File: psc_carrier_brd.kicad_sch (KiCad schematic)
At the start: 12 parts, among them J1 Conn_01x08_Pin, J2 Conn_01x05_Pin - 3.3v, J3 Conn_01x05_Pin - 5v, J4 6469028-1, J5 39301022, U1 WeMos_D1_mini, U5 OPA2197xDGK

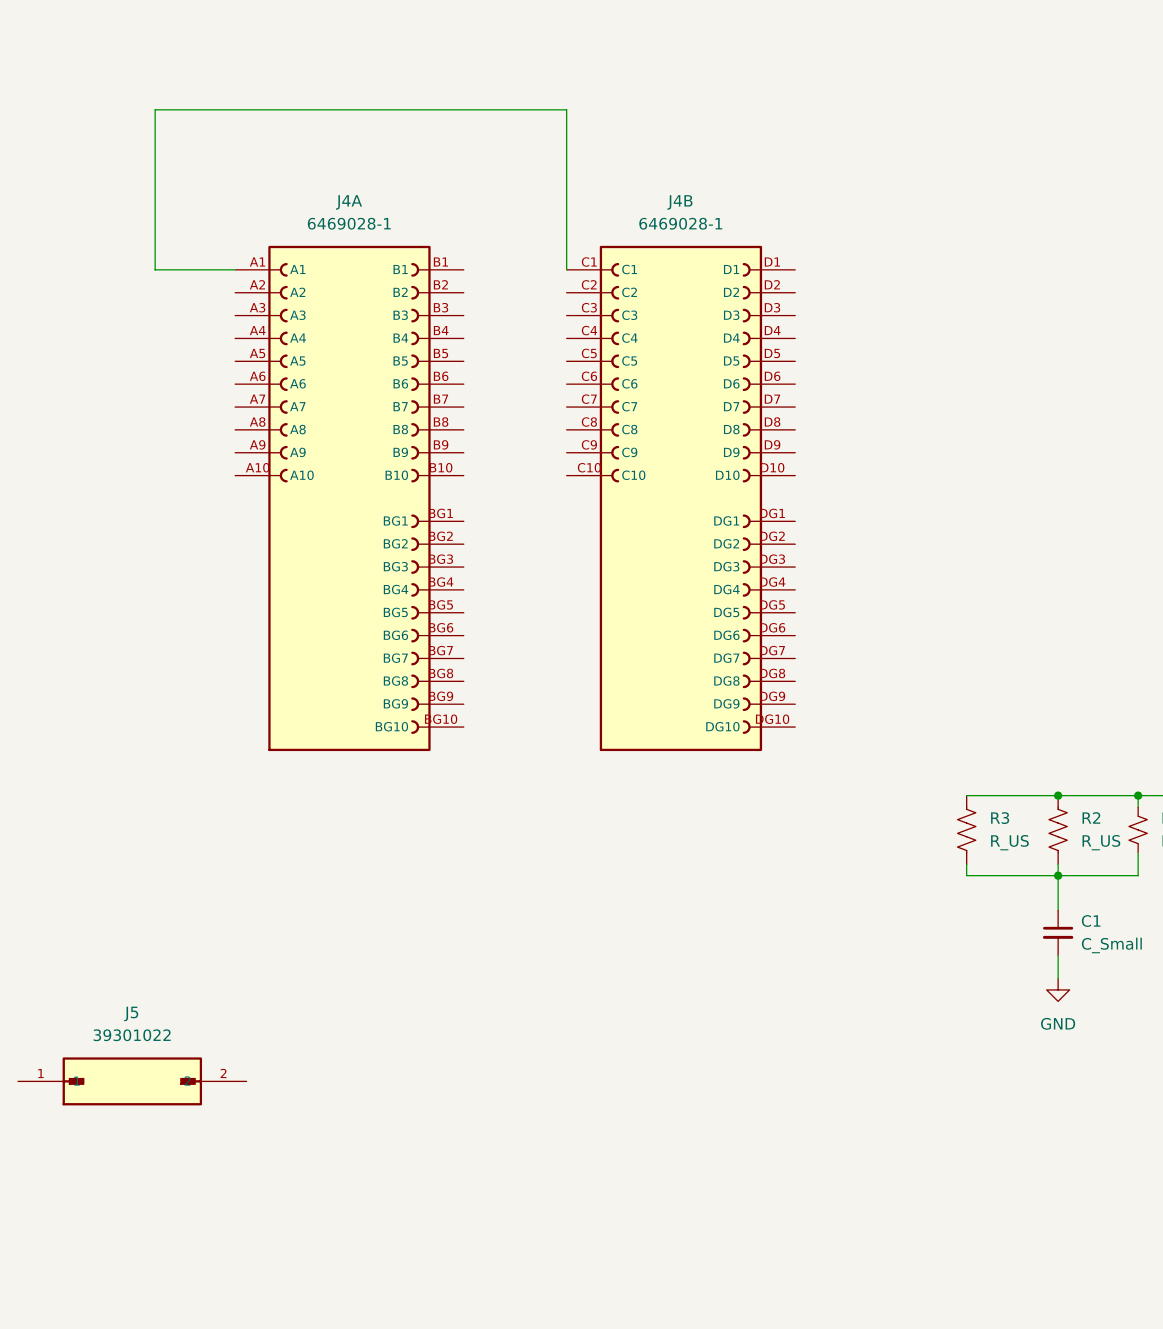
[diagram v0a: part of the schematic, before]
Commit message: Create 6469028-1 symbol
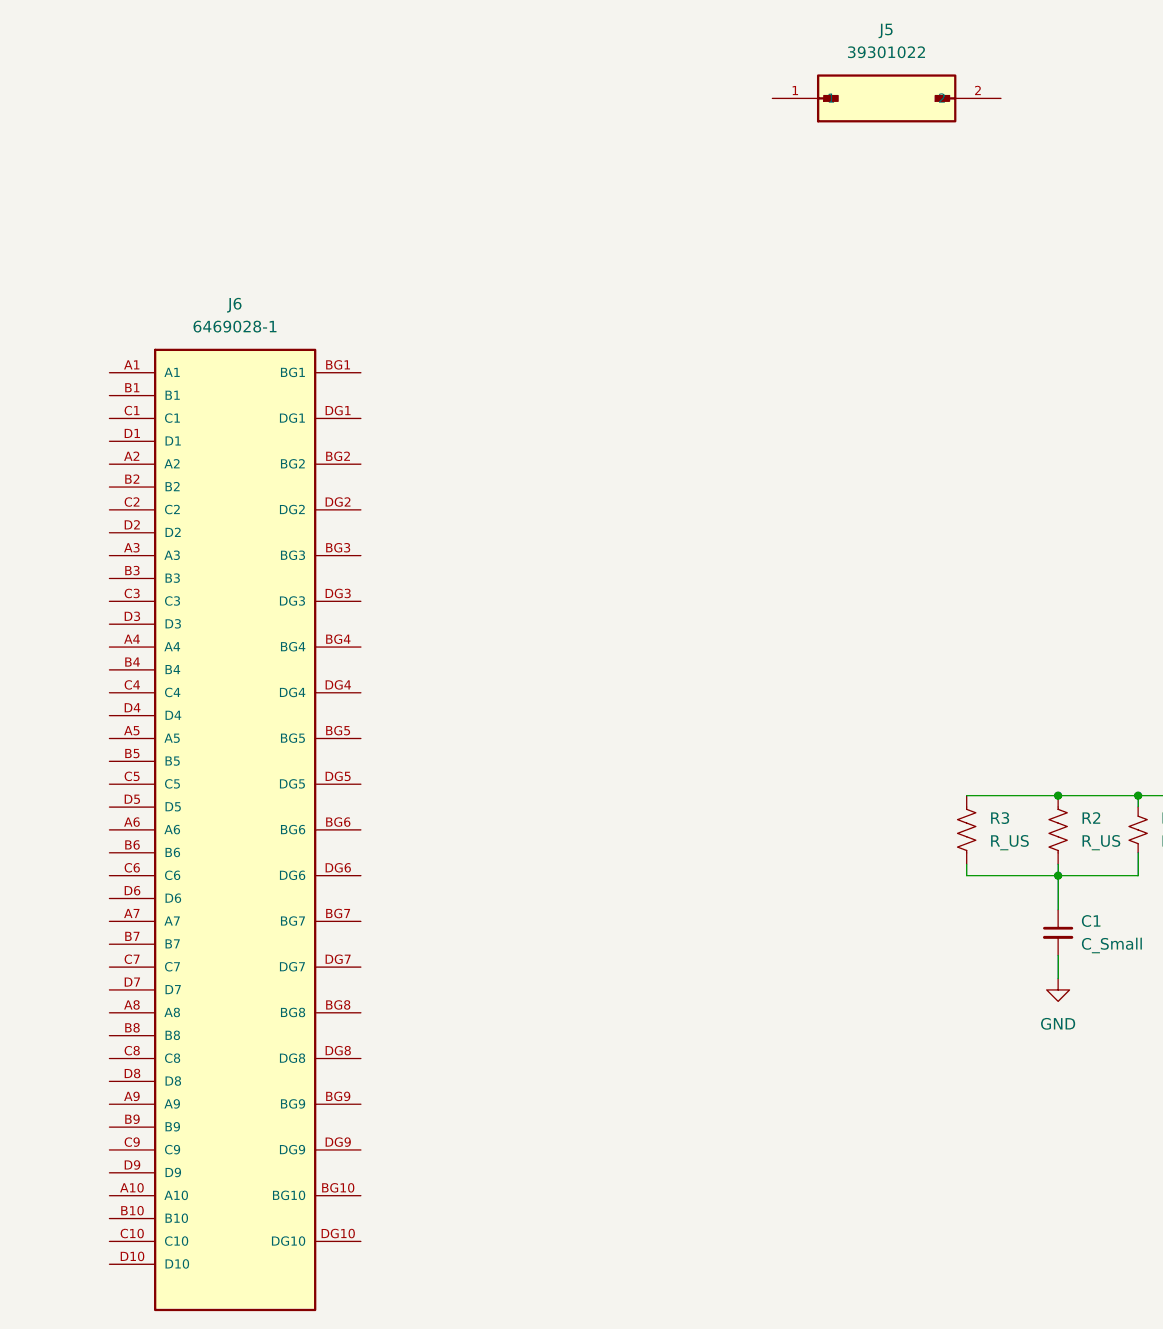
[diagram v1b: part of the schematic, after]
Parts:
- removed J4: 6469028-1, myparts:TE_6469028-1, symbol 6469028-1:6469028-1
- added J6: 6469028-1, 6469028-1:TE_6469028-1, symbol 6469028-1:6469028-1
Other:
- moved on the sheet: J5

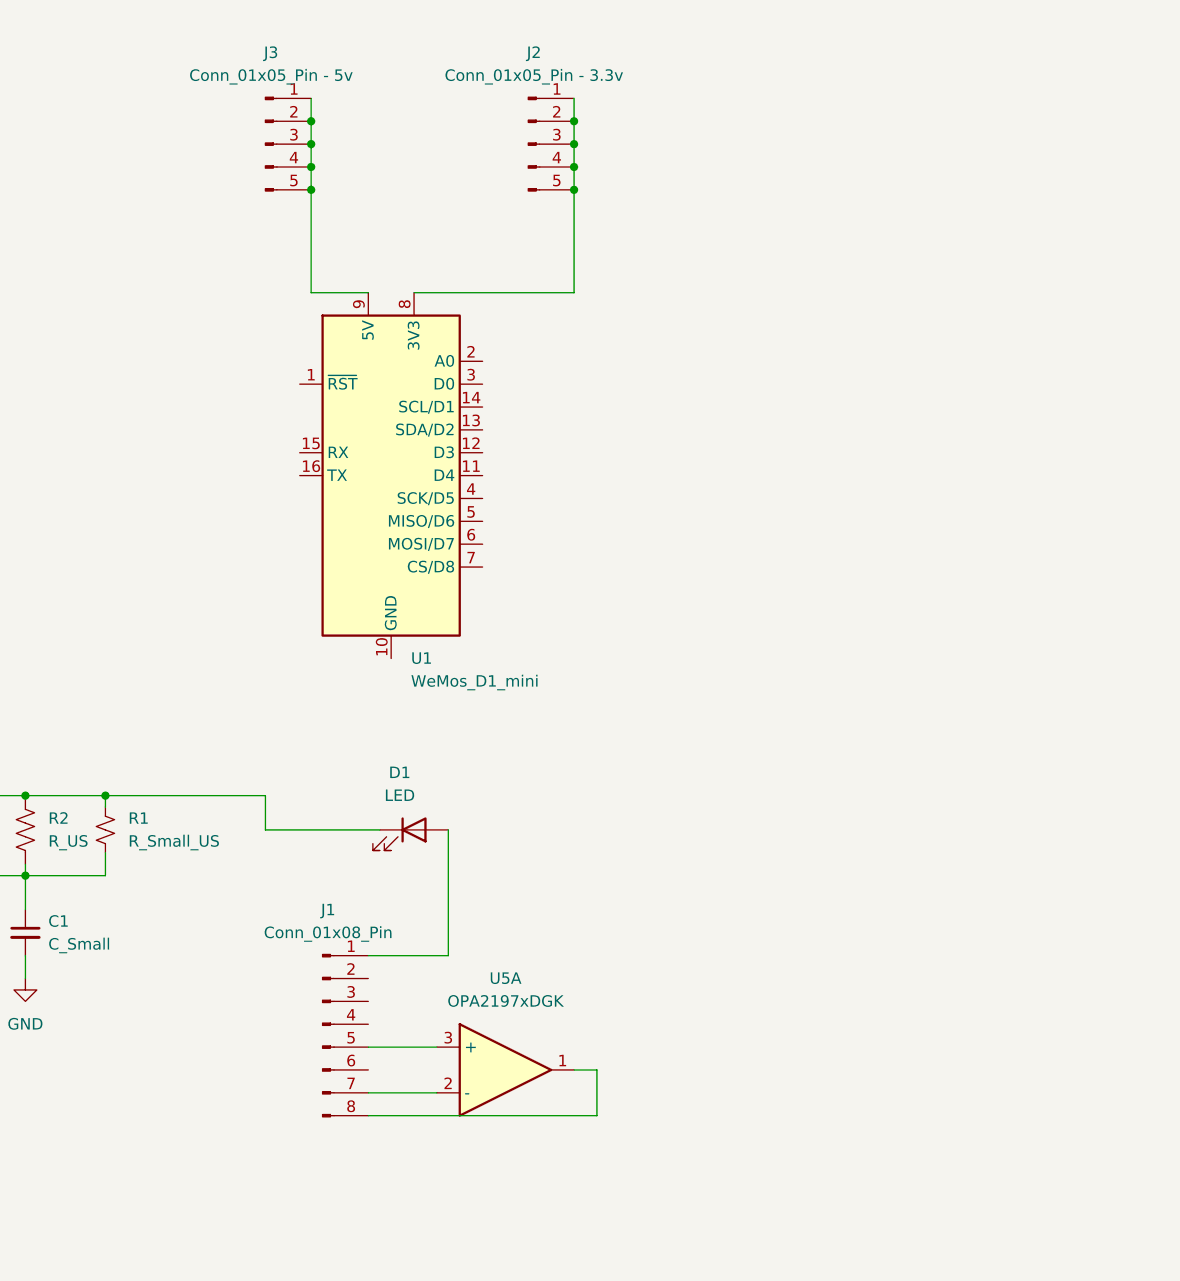
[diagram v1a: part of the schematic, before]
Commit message: Create custom NSLS2 worksheet
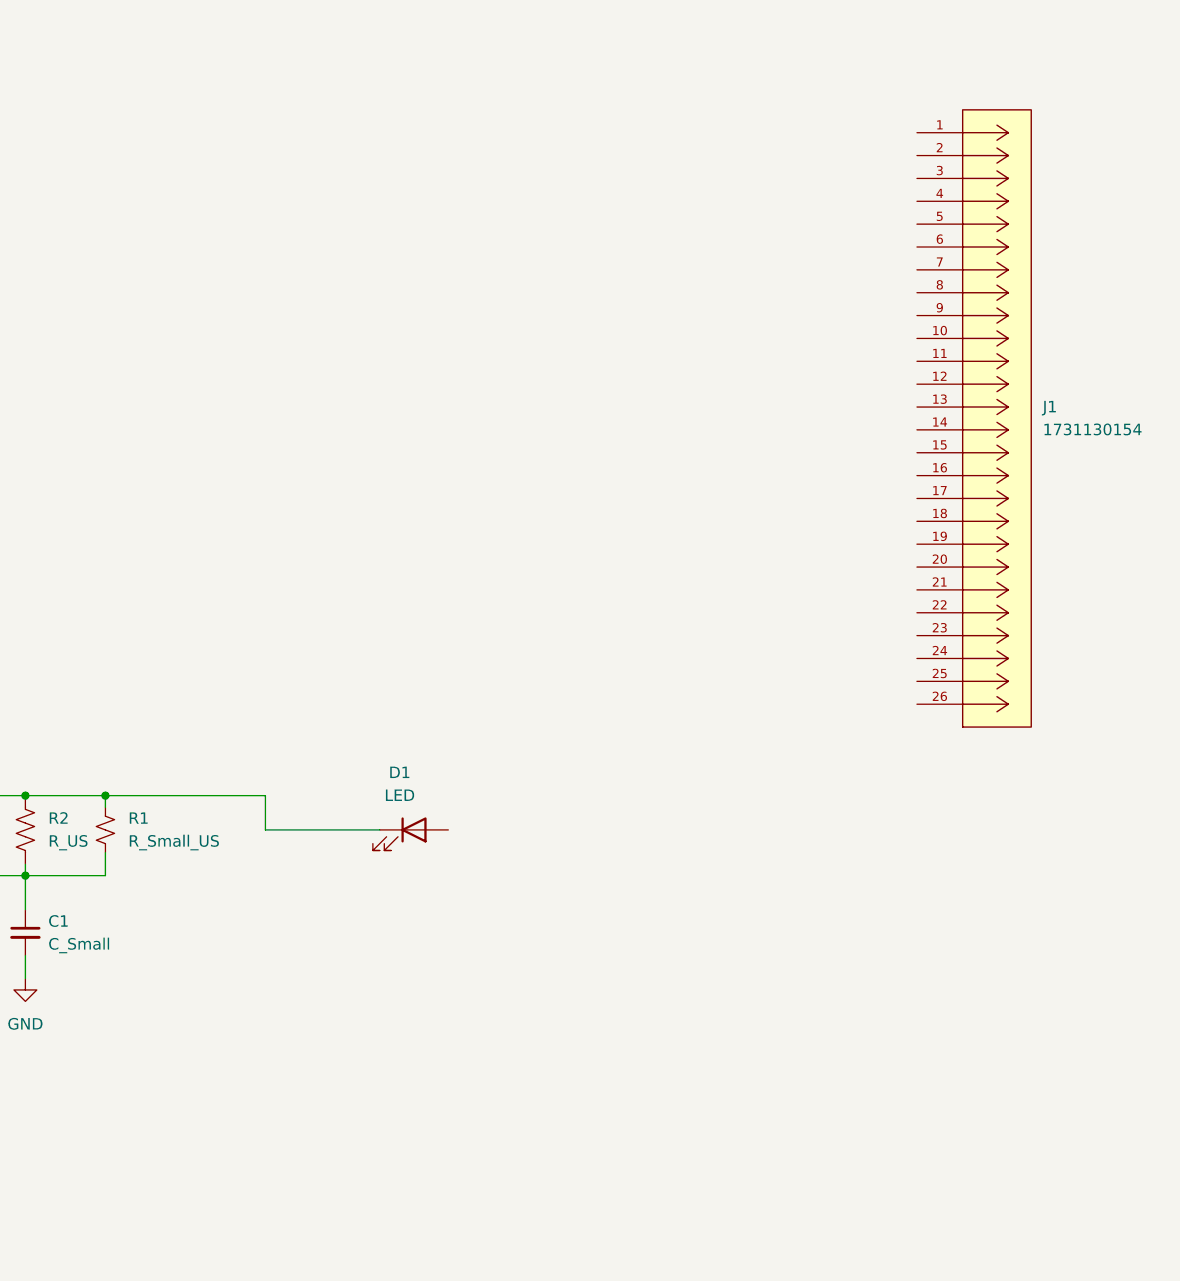
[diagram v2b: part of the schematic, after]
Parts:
- removed J1: Conn_01x08_Pin, Connector_PinHeader_2.54mm:PinHeader_1x08_P2.54mm_Vertical, symbol Connector:Conn_01x08_Pin
- removed J2: Conn_01x05_Pin - 3.3v, Connector_PinHeader_2.54mm:PinHeader_1x05_P2.54mm_Vertical_SMD_Pin1Left, symbol Connector:Conn_01x05_Pin
- removed J3: Conn_01x05_Pin - 5v, Connector_PinHeader_2.54mm:PinHeader_1x05_P2.54mm_Vertical_SMD_Pin1Left, symbol Connector:Conn_01x05_Pin
- removed U1: WeMos_D1_mini, Module:WEMOS_D1_mini_light, symbol MCU_Module:WeMos_D1_mini
- removed U5: OPA2197xDGK, Package_SO:VSSOP-8_3.0x3.0mm_P0.65mm, symbol Amplifier_Operational:OPA2197xDGK
- added J1: 1731130154, myparts:CONN_F15-26P135G0-5979_MOL, symbol 1731130154:1731130154
- J6: footprint 6469028-1:TE_6469028-1 -> myparts:TE_6469028-1

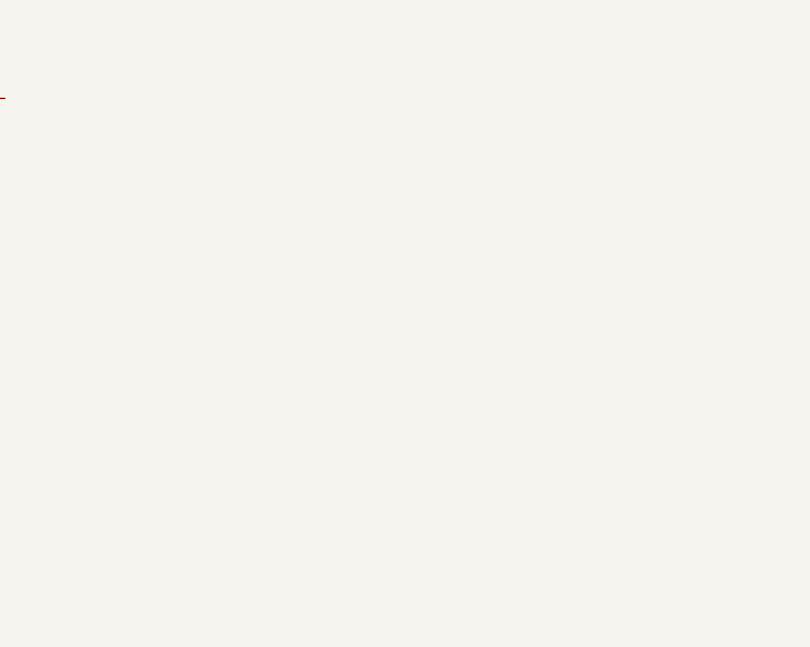
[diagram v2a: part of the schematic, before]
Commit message: Add symbol for PS connector
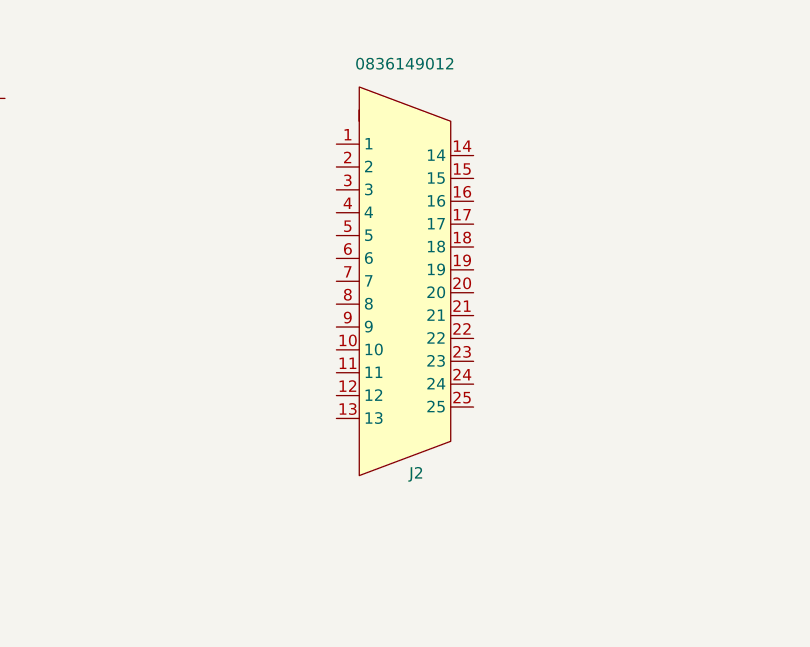
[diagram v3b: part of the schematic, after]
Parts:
- added J2: 0836149012, symbol 0836149012:0836149012
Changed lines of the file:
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@@
+	)
+	(symbol
+		(lib_id "0836149012:0836149012")
+		(at 207.01 40.64 0)
+		(unit 1)
+		(exclude_from_sim no)
+		(in_bom yes)
+		(on_board yes)
+		(dnp no)
+		(property "Reference" "J2"
+			(at 209.55 81.026 0)
+			(effects
+				(font
+					(size 1.27 1.27)
+				)
+			)
+		)
+		(property "Value" "0836149012"
+			(at 208.28 35.56 0)
+			(effects
+				(font
+					(size 1.27 1.27)
+				)
+			)
+		)
+		(property "Footprint" ""
+			(at 207.01 40.64 0)
+			(effects
+				(font
+					(size 1.27 1.27)
+				)
+				(hide yes)
+			)
+		)
+		(property "Datasheet" ""
+			(at 207.01 40.64 0)
+			(effects
+				(font
+					(size 1.27 1.27)
+				)
+				(hide yes)
+			)
+		)
+		(property "Description" ""
+			(at 207.01 40.64 0)
+			(effects
+				(font
+					(size 1.27 1.27)
+				)
+				(hide yes)
+			)
+		)
+		(pin "2"
+		)
+		(pin "25"
+		)
+		(pin "9"
+		)
+		(pin "4"
+		)
+		(pin "1"
+		)
+		(pin "10"
+		)
+		(pin "17"
+		)
+		(pin "22"
+		)
+		(pin "5"
+		)
+		(pin "3"
+		)
+		(pin "20"
+		)
+		(pin "6"
+		)
+		(pin "8"
+		)
+		(pin "24"
+		)
+		(pin "23"
+		)
+		(pin "21"
+		)
+		(pin "18"
+		)
+		(pin "19"
+		)
+		(pin "15"
+		)
+		(pin "12"
+		)
+		(pin "14"
+		)
+		(pin "13"
+		)
+		(pin "11"
+		)
+		(pin "16"
+		)
+		(pin "7"
+		)
+		(instances
+			(project ""
+				(path "/40891cc8-bf64-41f4-8f69-a607d7b280eb"
+					(reference "J2")
+					(unit 1)
+				)
+			)
+		)
 	)
 	(symbol

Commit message: Add footprint for PS connector
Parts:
- J2: footprint (none) -> myparts:0836149012
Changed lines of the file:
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@@
 			)
 		)
-		(property "Footprint" ""
+		(property "Footprint" "myparts:0836149012"
 			(at 207.01 40.64 0)
 			(effects
